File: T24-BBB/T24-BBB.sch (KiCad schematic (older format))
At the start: 38 parts, among them J25 9-16 In, J26 1-8 In, J27 17-24 In, J28 5V In, J29 OLED, J30 5V Select, J31 VIN2_V, J32 VIN3_V, J33 VIN1_V, J44 GPIO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

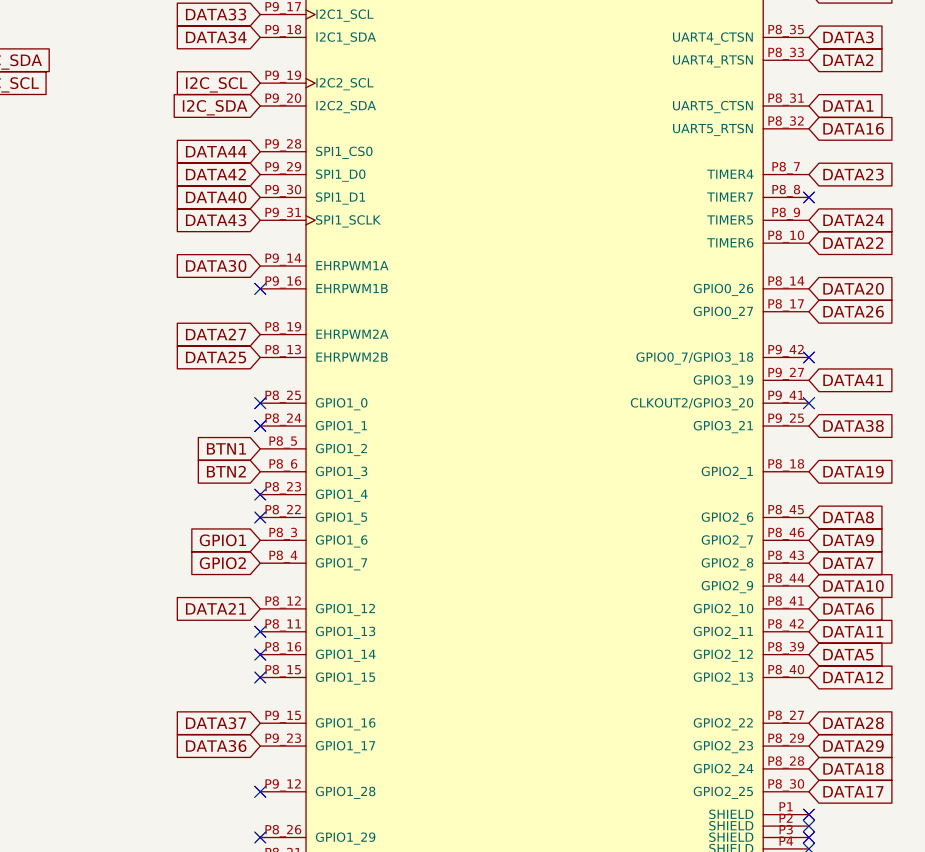
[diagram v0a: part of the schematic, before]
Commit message: SD Bus & Plugs
Fix GPIO and buttons sharing SD pins. Fix spacing on plugs as too tight.
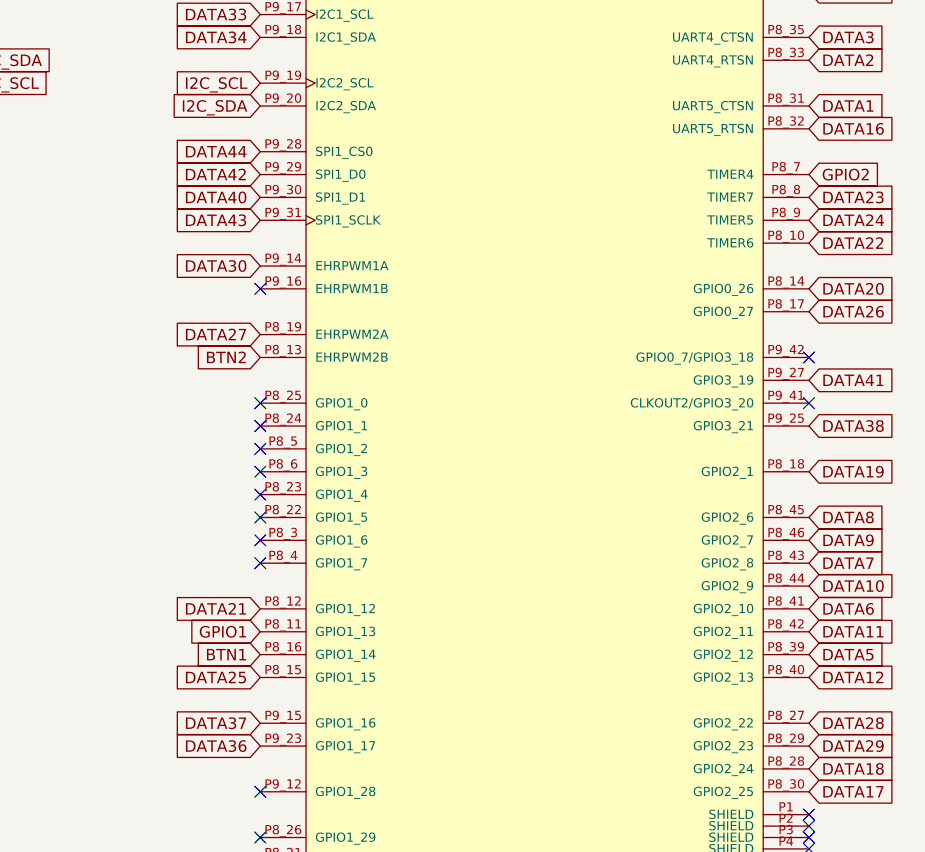
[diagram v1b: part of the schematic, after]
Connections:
- net BTN1: now also U11.P8_16 (GPIO1_14); no longer U11.P8_5 (GPIO1_2)
- net BTN2: now also U11.P8_13 (EHRPWM2B); no longer U11.P8_6 (GPIO1_3)
- net DATA23: now also U11.P8_8 (TIMER7); no longer U11.P8_7 (TIMER4)
- net DATA25: now also U11.P8_15 (GPIO1_15); no longer U11.P8_13 (EHRPWM2B)
- net GPIO1: now also U11.P8_11 (GPIO1_13); no longer U11.P8_3 (GPIO1_6)
- net GPIO2: now also U11.P8_7 (TIMER4); no longer U11.P8_4 (GPIO1_7)
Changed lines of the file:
@@
 Sheet 1 6
 Title "T24"
-Date "2021-03-13"
-Rev "0.7"
+Date "2021-03-14"
+Rev "0.7a"
 Comp "Lights On Windermere Avenue"
 Comment1 ""
@@
 Text GLabel 10750 3500 2    50   Input ~ 0
 DATA22
-Text GLabel 10750 3200 2    50   Input ~ 0
+Text GLabel 10750 3300 2    50   Input ~ 0
 DATA23
 Text GLabel 10750 3400 2    50   Input ~ 0
 DATA24
-Text GLabel 8350 4000 0    50   Input ~ 0
+Text GLabel 8350 5400 0    50   Input ~ 0
 DATA25
 Text GLabel 10750 3800 2    50   Input ~ 0
@@
 	0    1    1    0
 $EndComp
-Text GLabel 8350 4400 0    50   Input ~ 0
+Text GLabel 8350 5300 0    50   Input ~ 0
 BTN1
-Text GLabel 8350 4500 0    50   Input ~ 0
+Text GLabel 8350 4000 0    50   Input ~ 0
 BTN2
-Text GLabel 8350 4800 0    50   Input ~ 0
+Text GLabel 8350 5200 0    50   Input ~ 0
 GPIO1
-Text GLabel 8350 4900 0    50   Input ~ 0
+Text GLabel 10750 3200 2    50   Input ~ 0
 GPIO2
 $Comp
@@
 NoConn ~ 10750 800
 NoConn ~ 10750 900
-NoConn ~ 10750 3300
-NoConn ~ 8350 5200
-NoConn ~ 8350 5300
-NoConn ~ 8350 5400
 NoConn ~ 8350 6300
 NoConn ~ 8350 6200
-NoConn ~ 8350 4700
-NoConn ~ 8350 4600
-NoConn ~ 8350 4300
-NoConn ~ 8350 4200
 NoConn ~ 8350 6100
 NoConn ~ 8350 1200
@@
 V5
 NoConn ~ 8350 1100
+NoConn ~ 8350 4300
+NoConn ~ 8350 4200
+NoConn ~ 8350 4400
+NoConn ~ 8350 4500
+NoConn ~ 8350 4600
+NoConn ~ 8350 4700
+NoConn ~ 8350 4800
+NoConn ~ 8350 4900
 $EndSCHEMATC

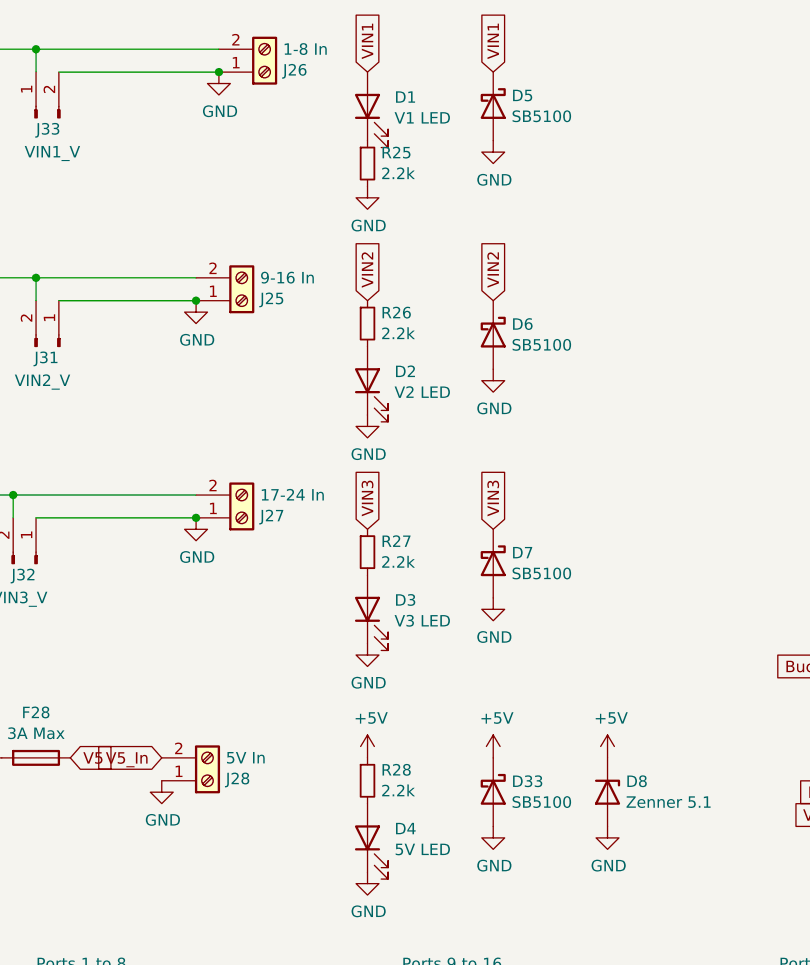
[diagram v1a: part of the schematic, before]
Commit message: Bump to 0.7b
Changed DMX connector. Tweaks.
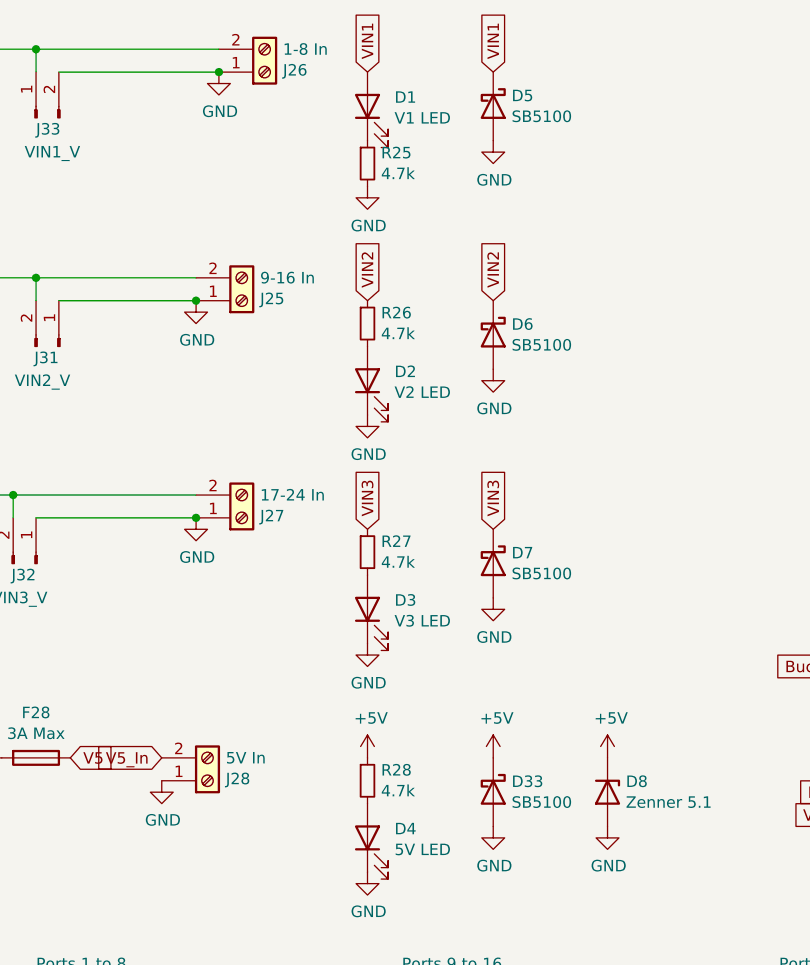
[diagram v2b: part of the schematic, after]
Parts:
- R25, R26, R27, R28: value 2.2k -> 4.7k; Description C17520 -> C17673
- U10: footprint Converter_DCDC:Converter_DCDC_muRata_OKI-78SR_Vertical -> Connector_PinHeader_2.54mm:PinHeader_1x03_P2.54mm_Vertical
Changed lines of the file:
@@
 Title "T24"
 Date "2021-03-14"
-Rev "0.7a"
+Rev "0.7b"
 Comp "Lights On Windermere Avenue"
 Comment1 ""
@@
 P 2400 1250
 F 0 "R25" H 2459 1296 50  0000 L CNN
-F 1 "2.2k" H 2459 1205 50  0000 L CNN
+F 1 "4.7k" H 2459 1205 50  0000 L CNN
 F 2 "3544again:R_0805_2012Metric" H 2400 1250 50  0001 C CNN
 F 3 "https://datasheet.lcsc.com/szlcsc/Uniroyal-Elec-0805W8F2201T5E_C17520.pdf" H 2400 1250 50  0001 C CNN
-F 4 "C17520" H 2400 1250 50  0001 C CNN "Description"
+F 4 "C17673" H 2400 1250 50  0001 C CNN "Description"
 	1    2400 1250
 	1    0    0    -1
@@
 P 2400 1950
 F 0 "R26" H 2459 1996 50  0000 L CNN
-F 1 "2.2k" H 2459 1905 50  0000 L CNN
+F 1 "4.7k" H 2459 1905 50  0000 L CNN
 F 2 "3544again:R_0805_2012Metric" H 2400 1950 50  0001 C CNN
 F 3 "https://datasheet.lcsc.com/szlcsc/Uniroyal-Elec-0805W8F2201T5E_C17520.pdf" H 2400 1950 50  0001 C CNN
-F 4 "C17520" H 2400 1950 50  0001 C CNN "Description"
+F 4 "C17673" H 2400 1950 50  0001 C CNN "Description"
 	1    2400 1950
 	1    0    0    -1
@@
 P 2400 3950
 F 0 "R28" H 2459 3996 50  0000 L CNN
-F 1 "2.2k" H 2459 3905 50  0000 L CNN
+F 1 "4.7k" H 2459 3905 50  0000 L CNN
 F 2 "3544again:R_0805_2012Metric" H 2400 3950 50  0001 C CNN
 F 3 "https://datasheet.lcsc.com/szlcsc/Uniroyal-Elec-0805W8F2201T5E_C17520.pdf" H 2400 3950 50  0001 C CNN
-F 4 "C17520" H 2400 3950 50  0001 C CNN "Description"
+F 4 "C17673" H 2400 3950 50  0001 C CNN "Description"
 	1    2400 3950
 	1    0    0    -1
@@
 P 2400 2950
 F 0 "R27" H 2459 2996 50  0000 L CNN
-F 1 "2.2k" H 2459 2905 50  0000 L CNN
+F 1 "4.7k" H 2459 2905 50  0000 L CNN
 F 2 "3544again:R_0805_2012Metric" H 2400 2950 50  0001 C CNN
 F 3 "https://datasheet.lcsc.com/szlcsc/Uniroyal-Elec-0805W8F2201T5E_C17520.pdf" H 2400 2950 50  0001 C CNN
-F 4 "C17520" H 2400 2950 50  0001 C CNN "Description"
+F 4 "C17673" H 2400 2950 50  0001 C CNN "Description"
 	1    2400 2950
 	1    0    0    -1
@@
 F 0 "U10" H 4750 3692 50  0000 C CNN
 F 1 "Buck" H 4750 3601 50  0000 C CNN
-F 2 "Converter_DCDC:Converter_DCDC_muRata_OKI-78SR_Vertical" H 4800 3200 50  0001 L CIN
-F 3 "https://power.murata.com/data/power/oki-78sr.pdf" H 4750 3450 50  0001 C CNN
+F 2 "Connector_PinHeader_2.54mm:PinHeader_1x03_P2.54mm_Vertical" H 4800 3200 50  0001 L CIN
+F 3 "" H 4750 3450 50  0001 C CNN
 	1    4750 3450
 	1    0    0    -1
